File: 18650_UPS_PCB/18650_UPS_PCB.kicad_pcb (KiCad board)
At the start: 4 copper layers, 90 x 22 mm, 54 parts, among them J1 USB_B_Micro, J2 Conn_02x04_Odd_Even, J3 USB_A, SW1 SW_SPDT, SW2 ALPSALPINE_SKRHADE011, SW3 SW_SPDT, SW4 SW_SPDT, SW5 SW_SPDT, U1 STLINK-V3MINI, U10 LR9102G-xx, U2 R5478, U3 STC4054, U4 FS8205A, U5 ME2188Cxx, U6 XC9236Axx, U7 INA219AxD, U8 SSD1306_128_32, U9 STM32F030F4Px

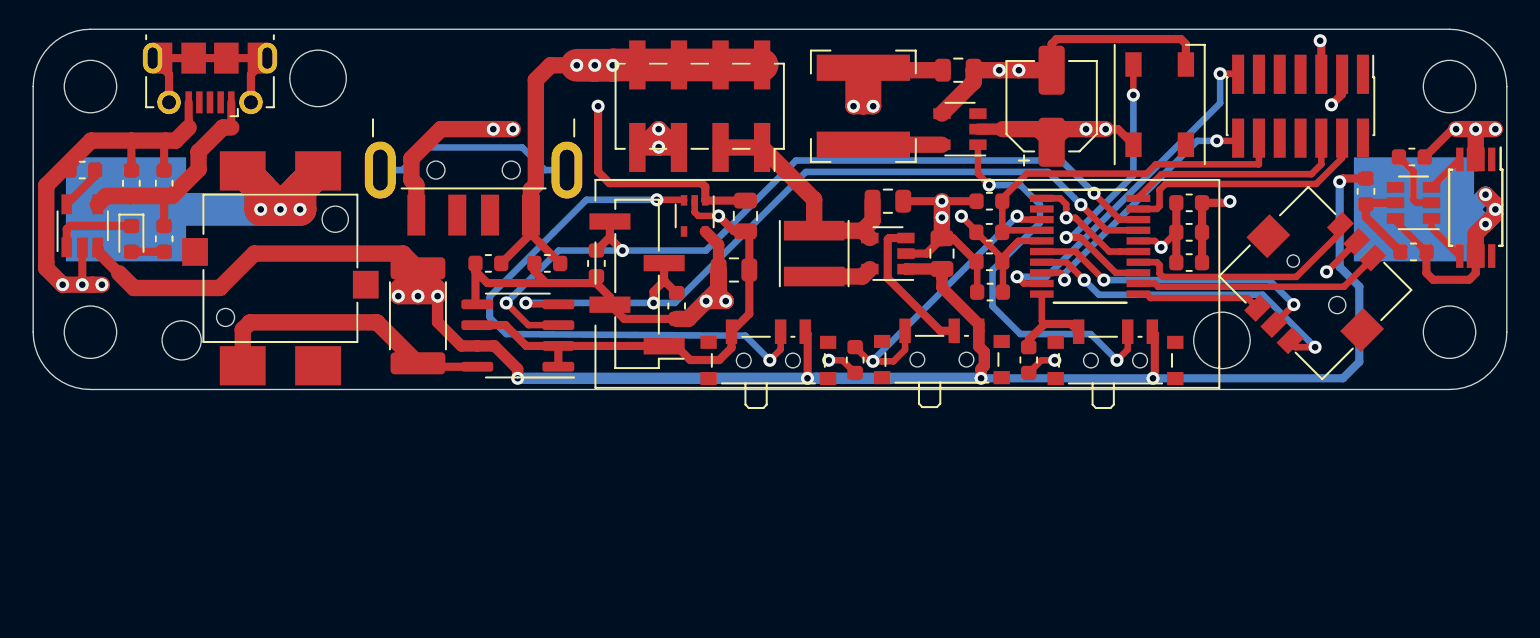
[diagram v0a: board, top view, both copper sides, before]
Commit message: base for v2 with new bms and sense ic
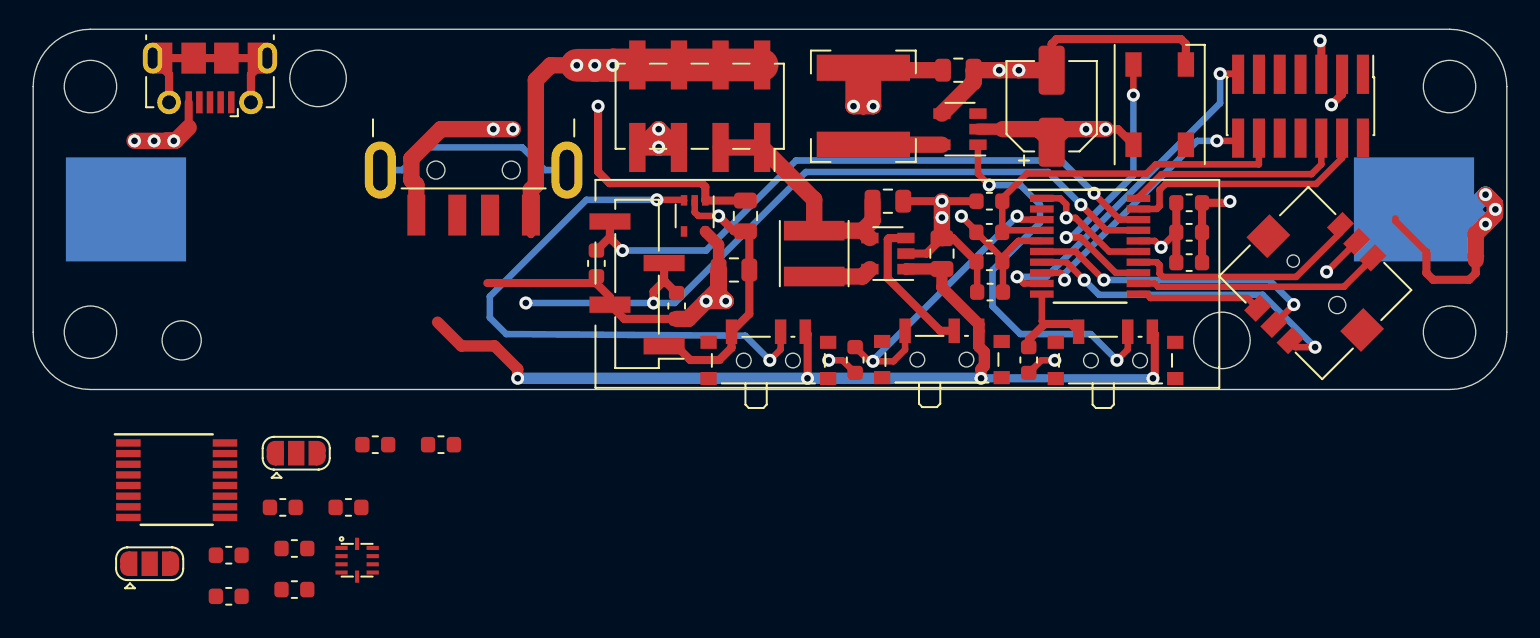
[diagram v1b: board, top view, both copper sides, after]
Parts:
- removed C12: 10 uF, Capacitor_SMD:C_0603_1608Metric
- removed C13: 100 nF, Capacitor_SMD:C_0603_1608Metric
- removed C2: 10 nF, Capacitor_SMD:C_0603_1608Metric
- removed C3: 1 uF, Capacitor_SMD:C_0603_1608Metric
- removed D1: LED_CHRG, LED_SMD:LED_0603_1608Metric
- removed R2: 0.1 Ohm, Resistor_SMD:R_2512_6332Metric
- removed R3, R4: 1 kOhm, Resistor_SMD:R_0603_1608Metric
- removed R5: 1.25 kOhm, Resistor_SMD:R_0603_1608Metric
- removed SW1: SW_SPDT, CUSTOM_FOOTPRINTS:ALPS_SPEF210101
- removed U3: STC4054, Package_TO_SOT_SMD:TSOT-23-5
- removed U4: FS8205A, Package_SO:TSSOP-8_4.4x3mm_P0.65mm
- removed U7: INA219AxD, Package_SO:SOIC-8_3.9x4.9mm_P1.27mm
- added C10: 1 uF, Capacitor_SMD:C_0603_1608Metric, F.Cu at (136.1, 103.4)
- added C11: 100 nF, Capacitor_SMD:C_0603_1608Metric, F.Cu at (141.7, 99.6)
- added C20: 10 uF, Capacitor_SMD:C_0603_1608Metric, F.Cu at (132.8, 108.8)
- added C21: 2.2 uF, Capacitor_SMD:C_0603_1608Metric, F.Cu at (136.8, 105.9)
- added JP1: SolderJumper_3_Open, Jumper:SolderJumper-3_P1.3mm_Open_RoundedPad1.0x1.5mm, F.Cu at (127.9, 106.8)
- added JP2: SolderJumper_3_Open, Jumper:SolderJumper-3_P1.3mm_Open_RoundedPad1.0x1.5mm, F.Cu at (136.9, 100.1)
- added R8: 10 kOhm, Resistor_SMD:R_0603_1608Metric, F.Cu at (145.7, 99.6)
- added R9: 10 kOhm, Resistor_SMD:R_0603_1608Metric, F.Cu at (136.8, 108.4)
- added U11: MP2667, CUSTOM_FOOTPRINTS:QFN-10-MP2667, F.Cu at (140.6, 106.6)
- R1: value 330 Ohm -> 10 kOhm
- U2: value R5478 -> INA260; footprint Package_TO_SOT_SMD:SOT-23-6 -> Package_SO:TSSOP-16_4.4x5mm_P0.65mm
- moved U2 77.4 mm to (129.6, 101.7), turned to 0 degrees
- moved R1 65.1 mm to (140.1, 103.4), turned to 0 degrees
- moved C1 23.5 mm to (132.8, 106.3), turned to 0 degrees
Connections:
- BT1 pad 2: -BATT -> GND
- C1 pad 1: -BATT -> +3.3VA
- C1 pad 2: VCC -> GND
- C14 pad 1: GNDD -> GND
- C15 pad 1: GNDD -> GND
- C16 pad 1: GNDD -> GND
- C17 pad 1: GNDD -> GND
- C18 pad 2: GNDD -> GND
- C19 pad 2: GNDD -> GND
- C4 pad 1: Shunt- -> IN-
- C4 pad 2: GNDD -> GND
- C5 pad 1: Shunt- -> IN-
- C5 pad 2: GNDD -> GND
- C6 pad 1: Shunt- -> IN-
- C6 pad 2: GNDD -> GND
- C7 pad 2: GNDD -> GND
- C8 pad 2: GNDD -> GND
- C9 pad 2: GNDD -> GND
- D2 pad 2: Net-(D2-Pad2) -> (no net)
- D2 pad 3: GNDD -> GND
- J1 pad 1: VCC -> Net-(C10-Pad1)
- J1 pad 2: Net-(J1-Pad2) -> (no net)
- J1 pad 3: Net-(J1-Pad3) -> (no net)
- J1 pad 4: Net-(J1-Pad4) -> (no net)
- J1 pad 5: -BATT -> GND
- J2 pad 2: GNDD -> GND
- J2 pad 4: GNDD -> GND
- J2 pad 6: GNDD -> GND
- J2 pad 8: GNDD -> GND
- J3 pad 2: Net-(J3-Pad2) -> (no net)
- J3 pad 3: Net-(J3-Pad3) -> (no net)
- J3 pad 4: GNDD -> GND
- L1 pad 1: Shunt- -> IN-
- R1 pad 1: Net-(C2-Pad2) -> +3.3VA
- R1 pad 2: Shunt- -> PF0
- R6 pad 2: GNDD -> GND
- R7 pad 2: GNDD -> GND
- SW2 pad 5: GNDD -> GND
- SW3 pad 3: Shunt- -> IN-
- SW4 pad 3: Shunt- -> IN-
- SW5 pad 1: GNDD -> GND
- SW5 pad 3: Shunt- -> IN-
- U1 pad 1: Net-(U1-Pad1) -> (no net)
- U1 pad 10: Net-(U1-Pad10) -> (no net)
- U1 pad 11: Net-(U1-Pad11) -> (no net)
- U1 pad 2: Net-(U1-Pad2) -> (no net)
- U1 pad 5: GNDD -> GND
- U1 pad 7: Net-(U1-Pad7) -> (no net)
- U1 pad 8: Net-(U1-Pad8) -> (no net)
- U1 pad 9: Net-(U1-Pad9) -> (no net)
- U10 pad 1: Shunt- -> IN-
- U10 pad 2: GNDD -> GND
- U10 pad 4: Net-(U10-Pad4) -> (no net)
- U2 pad 1: Net-(U2-Pad1) -> IN+
- U2 pad 2: Net-(R4-Pad2) -> IN+
- U2 pad 3: Net-(U2-Pad3) -> IN+
- U2 pad 5: Net-(C2-Pad2) -> Net-(JP1-Pad2)
- U2 pad 6: -BATT -> GND
- U5 pad 3: Net-(U5-Pad3) -> (no net)
- U5 pad 4: GNDD -> GND
- U6 pad 1: Shunt- -> IN-
- U6 pad 2: GNDD -> GND
- U8 pad 1: GNDD -> GND
- U9 pad 1: GNDD -> GND
- U9 pad 15: GNDD -> GND
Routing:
- net Shunt-: track 190.8 -> 0.00 mm, vias 11 -> 0
- net -BATT: track 143.4 -> 0.00 mm, vias 6 -> 0
- net IN-: track 0.00 -> 132.6 mm, vias 0 -> 7
- net GND: track 0.00 -> 128.6 mm, vias 0 -> 20
- net GNDD: track 123.0 -> 0.00 mm, vias 17 -> 0
- net Net-(BT1-Pad1): track 25.2 -> 0.00 mm, vias 3 -> 0
- net Shunt+: track 17.8 -> 0.00 mm
- net VCC: track 14.1 -> 0.00 mm
- net I2C1_SDA: track 50.7 -> 38.6 mm, vias 3 -> 2
- net +3.3VA: track 97.5 -> 91.8 mm
- net Net-(C2-Pad2): track 5.62 -> 0.00 mm
- net Net-(D1-Pad1): track 5.14 -> 0.00 mm
- net Net-(R4-Pad2): track 4.17 -> 0.00 mm
- net Net-(U2-Pad1): track 3.01 -> 0.00 mm
- net Net-(R5-Pad1): track 2.81 -> 0.00 mm
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- added copper zone on In1.Cu, net GND
- removed copper zone on In1.Cu, net GNDD

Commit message: savepoint before messing up pcbnew
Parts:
- removed D2: WS2812B, LED_SMD:LED_WS2812B_PLCC4_5.0x5.0mm_P3.2mm
- removed L2: 1.5 uH, Inductor_SMD:L_Taiyo-Yuden_MD-4040
- removed R12, R13, R17, R6, R7: 10 kOhm, Resistor_SMD:R_0603_1608Metric
- removed SW2: ALPSALPINE_SKRHADE011, CUSTOM_FOOTPRINTS:SKRHADE011
- removed SW3, SW4, SW5: SW_SPDT, Button_Switch_SMD:SW_SPDT_PCM12
- removed U6: XC9236Axx, Package_TO_SOT_SMD:SOT-23-5
- removed U8: SSD1306_128_32, Connector_PinHeader_2.54mm:PinHeader_1x04_P2.54mm_Vertical_SMD_Pin1Left
- removed U9: STM32F030F4Px, Package_SO:TSSOP-20_4.4x6.5mm_P0.65mm
- added C12: 100 nF, Capacitor_SMD:C_0603_1608Metric, F.Cu at (207.2, 161.4)
- added C13: 2.2 uF, Capacitor_SMD:C_0603_1608Metric, F.Cu at (187.8, 162.7)
- added C2: 1 uF, Capacitor_SMD:C_0603_1608Metric, F.Cu at (227.2, 157.7)
- added C3: 1 uF, Capacitor_SMD:C_0603_1608Metric, F.Cu at (199.2, 158.9)
- added J4: Conn_01x02, Connector_PinSocket_2.54mm:PinSocket_1x02_P2.54mm_Vertical, F.Cu at (228.6, 151.6)
- added J5: Conn_01x02, Connector_PinSocket_2.54mm:PinSocket_1x02_P2.54mm_Vertical, F.Cu at (240.4, 137.8)
- added J6: Conn_01x02, Connector_PinSocket_2.54mm:PinSocket_1x02_P2.54mm_Vertical, F.Cu at (222.9, 157.5)
- added JP3: EA_ADR, Jumper:SolderJumper-3_P1.3mm_Open_RoundedPad1.0x1.5mm, F.Cu at (188.7, 159.4)
- added JP4: TPS_LBI, Jumper:SolderJumper-3_P1.3mm_Open_RoundedPad1.0x1.5mm, F.Cu at (194.3, 159.4)
- added R2: 10 kOhm, Resistor_SMD:R_0603_1608Metric, F.Cu at (232.0, 146.0)
- added S1: TM-2027, CUSTOM_FOOTPRINTS:TM-2027, F.Cu at (223.0, 143.6)
- added SW1: SW_DIP_x02, CUSTOM_FOOTPRINTS:TS6637TP-4P, F.Cu at (180.5, 160.7)
- added U3: EA_DOGS164N-A, CUSTOM_FOOTPRINTS:EA_DOGS164N-A, F.Cu at (183.9, 155.6)
- added U4: TPS61032, Package_SO:HTSSOP-16-1EP_4.4x5mm_P0.65mm_EP3.4x5mm, F.Cu at (234.0, 141.4)
- C15: value 200 nF -> 220 uF; footprint Capacitor_SMD:C_0603_1608Metric -> Capacitor_Tantalum_SMD:CP_EIA-7343-43_Kemet-X_Pad2.25x2.55mm_HandSolder
- C16: value 200 nF -> 100 nF
- C17: value 4.7 uF -> 100 nF
- C18: value 10 nF -> 1 uF
- C19: value 1 uF -> 100 nF
- C4: value 4.7 uF -> 10 uF; footprint Capacitor_SMD:C_0805_2012Metric -> Capacitor_SMD:C_0603_1608Metric
- C5: value 10 uF -> 0.1 uF; footprint Capacitor_SMD:C_0805_2012Metric -> Capacitor_SMD:C_0603_1608Metric
- C7: value 100 uF -> 4.7 uF; footprint Capacitor_SMD:CP_Elec_5x5.4 -> Capacitor_SMD:C_0603_1608Metric
- C9: value 10 uF -> 100 nF; footprint Capacitor_SMD:C_0805_2012Metric -> Capacitor_SMD:C_0603_1608Metric
- J2: value Conn_02x04_Odd_Even -> Conn_01x02; footprint Connector_PinSocket_2.54mm:PinSocket_2x04_P2.54mm_Vertical_SMD -> Connector_PinSocket_2.54mm:PinSocket_1x02_P2.54mm_Vertical
- JP1: value SolderJumper_3_Open -> INA_ADR_0
- JP2: value SolderJumper_3_Open -> INA_ADR_1
- L1: value 22 uH -> 6.8 uH; footprint Inductor_SMD:L_Bourns-SRN6028 -> Inductor_SMD:L_10.4x10.4_H4.8
- U5: value ME2188Cxx -> STM32L151RCTx; footprint Package_TO_SOT_SMD:SOT-23-5 -> Package_QFP:LQFP-64_10x10mm_P0.5mm
- moved J2 97.0 mm to (218.3, 157.5), turned to 0 degrees
- moved C5 87.5 mm to (207.2, 158.9)
- moved C7 84.1 mm to (199.2, 161.4), turned to 0 degrees
- moved C19 82.9 mm to (244.7, 139.2), turned to 0 degrees
- moved L1 82.5 mm to (236.7, 129.5), turned to 0 degrees
- moved C9 82.4 mm to (203.2, 161.4)
- moved C18 80.2 mm to (244.7, 136.7), turned to 0 degrees
- moved C17 79.1 mm to (211.2, 161.4), turned to 0 degrees
- moved C14 79.1 mm to (191.9, 162.7)
- moved C4 75.9 mm to (203.2, 158.9), turned to 0 degrees
- moved C16 75.0 mm to (211.2, 158.9), turned to 0 degrees
- moved C15 70.4 mm to (221.1, 152.2), turned to 0 degrees
- moved U5 68.2 mm to (223.2, 130.8), turned to 0 degrees
- moved C20 34.9 mm to (148.3, 140.1)
- moved R9 34.9 mm to (152.3, 139.7)
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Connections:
- C1 pad 1: +3.3VA -> +3V3
- C14 pad 1: GND -> +3V3
- C14 pad 2: NRST -> GND
- C15 pad 1: GND -> +5V
- C15 pad 2: +3.3VA -> GND
- C16 pad 1: GND -> +3V3
- C16 pad 2: +3.3VA -> GND
- C17 pad 1: GND -> +3V3
- C17 pad 2: +3.3VA -> GND
- C18 pad 1: +3.3VA -> +3V3
- C19 pad 1: +3.3VA -> IN-
- C5 pad 1: IN- -> NRST
- C7 pad 1: +5V -> +3V3
- C8 pad 1: +3.3VA -> +3V3
- JP1 pad 3: +3.3VA -> +3V3
- JP2 pad 1: +3.3VA -> +3V3
- R1 pad 1: +3.3VA -> +3V3
- R1 pad 2: PF0 -> INA-ALERT
- U1 pad 3: +3.3VA -> +3V3
- U10 pad 3: LDOCE -> IN-
- U10 pad 5: +3.3VA -> +3V3
- U11 pad 3: (no net) -> MP-INT
- U2 pad 10: +3.3VA -> +3V3
- U2 pad 7: PF0 -> INA-ALERT
- U5 pad 1: BoostCE -> (no net)
- U5 pad 2: +5V -> (no net)
- U5 pad 4: GND -> (no net)
- U5 pad 5: Net-(L1-Pad2) -> (no net)
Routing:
- net +3V3: track 14.6 -> 106.4 mm, vias 0 -> 5
- net +3.3VA: track 91.8 -> 0.00 mm, vias 5 -> 0
- net LDOCE: track 35.8 -> 0.00 mm, vias 2 -> 0
- net IN-: track 132.6 -> 168.3 mm, vias 7 -> 9

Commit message: all parts on pcb
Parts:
- removed J3: USB_A, Connector_USB:USB_A_CNCTech_1001-011-01101_Horizontal
- JP3, JP4: moved to B.Cu
- U3: value EA_DOGS164N-A -> EA_DOGS104N-A; footprint CUSTOM_FOOTPRINTS:EA_DOGS164N-A -> CUSTOM_FOOTPRINTS:EA_DOGS104N-A
- moved C2 110.6 mm to (150.0, 78.4), turned to 180 degrees
- moved C18 103.3 mm to (148.3, 99.5), turned to 270 degrees
- moved JP3 102.2 mm to (129.7, 76.0), turned to 180 degrees
- moved R2 100.6 mm to (142.8, 99.5), turned to 90 degrees
- moved C16 99.7 mm to (136.5, 92.8), turned to 180 degrees
- moved J2 97.0 mm to (165.8, 75.9), turned to 90 degrees
- moved C14 96.8 mm to (142.3, 79.5), turned to 90 degrees
- moved J6 92.8 mm to (178.5, 75.9), turned to 90 degrees
- moved J5 92.1 mm to (172.2, 75.9), turned to 90 degrees
- moved C3 91.7 mm to (155.2, 78.4), turned to 180 degrees
- moved C12 91.4 mm to (156.4, 85.3)
- moved U5 87.7 mm to (146.0, 89.1), turned to 90 degrees
- moved J4 87.4 mm to (184.9, 75.9), turned to 90 degrees
- moved C17 86.6 mm to (150.6, 99.5), turned to 270 degrees
- moved C5 85.8 mm to (145.2, 99.5), turned to 270 degrees
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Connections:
- C10 pad 1: Net-(C10-Pad1) -> VBUS
- J1 pad 1: Net-(C10-Pad1) -> VBUS
- R8 pad 1: (no net) -> VBUS
- U11 pad 1: Net-(C10-Pad1) -> VBUS
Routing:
- net IN-: track 168.3 -> 0.00 mm, vias 9 -> 0
- net GND: track 128.6 -> 0.00 mm, vias 20 -> 0
- net +3V3: track 106.4 -> 0.00 mm, vias 5 -> 0
- net +5V: track 68.2 -> 0.00 mm, vias 6 -> 0
- net I2C1_SCL: track 46.1 -> 0.00 mm, vias 3 -> 0
- net I2C1_SDA: track 38.6 -> 0.00 mm, vias 2 -> 0
- net BoostCE: track 24.7 -> 0.00 mm, vias 2 -> 0
- net NRST: track 22.7 -> 0.00 mm
- net USART1_RX: track 21.4 -> 0.00 mm, vias 2 -> 0
- net PA1: track 20.6 -> 0.00 mm, vias 2 -> 0
- net PF1: track 19.0 -> 0.00 mm, vias 2 -> 0
- net PA0: track 18.5 -> 0.00 mm, vias 2 -> 0
- net PA7: track 17.7 -> 0.00 mm, vias 2 -> 0
- net USART1_TX: track 16.1 -> 0.00 mm, vias 2 -> 0
- net SWDIO: track 15.5 -> 0.00 mm
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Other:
- board size 90 x 22 mm -> 90 x 27.5 mm

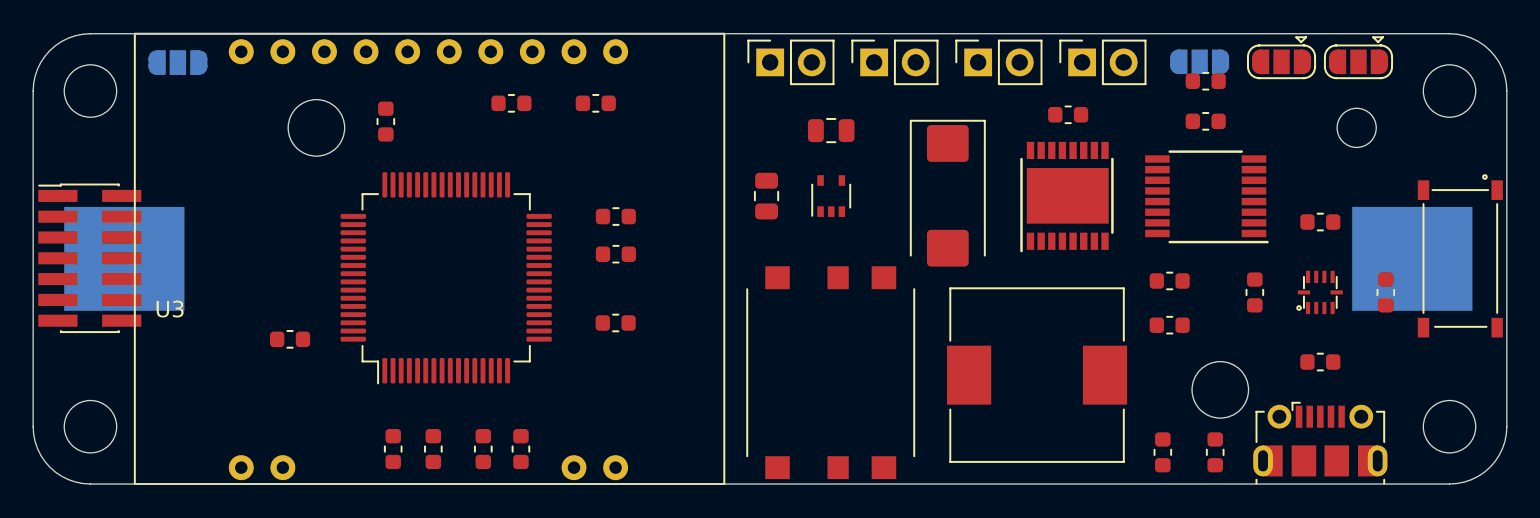
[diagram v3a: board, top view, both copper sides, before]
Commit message: placed all components
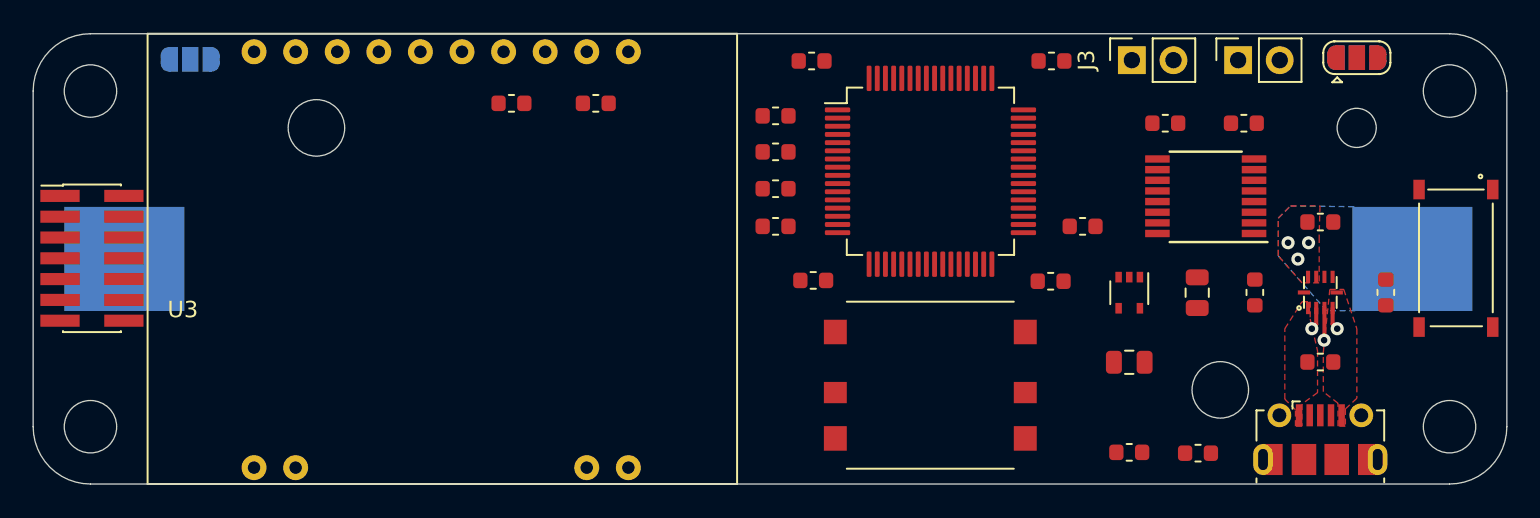
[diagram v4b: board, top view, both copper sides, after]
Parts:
- removed C13: 2.2 uF, Capacitor_SMD:C_0603_1608Metric
- removed C15: 220 uF, Capacitor_Tantalum_SMD:CP_EIA-7343-43_Kemet-X_Pad2.25x2.55mm_HandSolder
- removed C19: 100 nF, Capacitor_SMD:C_0603_1608Metric
- removed C4: 10 uF, Capacitor_SMD:C_0603_1608Metric
- removed J4, J5, J6: Conn_01x02, Connector_PinSocket_2.54mm:PinSocket_1x02_P2.54mm_Vertical
- removed JP4: TPS_LBI, Jumper:SolderJumper-3_P1.3mm_Open_RoundedPad1.0x1.5mm
- removed L1: 6.8 uH, Inductor_SMD:L_10.4x10.4_H4.8
- removed U4: TPS61032, Package_SO:HTSSOP-16-1EP_4.4x5mm_P0.65mm_EP3.4x5mm
- added J3: Conn_01x02, Connector_PinSocket_2.54mm:PinSocket_1x02_P2.54mm_Vertical, F.Cu at (187.9, 75.8)
- JP2: moved to B.Cu
- moved C14 40.8 mm to (183.0, 75.8), turned to 0 degrees
- moved C16 36.1 mm to (168.3, 75.8)
- moved R2 31.0 mm to (166.2, 79.2), turned to 0 degrees
- moved U5 30.3 mm to (175.6, 82.6), turned to 0 degrees
- moved J2 28.6 mm to (194.4, 75.8)
- moved C7 28.6 mm to (184.9, 86.0)
- moved C5 27.7 mm to (166.2, 81.4), turned to 180 degrees
- moved C6 27.0 mm to (191.9, 90.0), turned to 270 degrees
- moved C12 26.8 mm to (182.9, 89.3)
- moved C18 23.9 mm to (166.2, 83.7), turned to 180 degrees
- moved C8 23.1 mm to (187.8, 94.2), turned to 180 degrees
- moved C17 20.7 mm to (166.2, 86.0), turned to 180 degrees
- moved U10 19.1 mm to (187.8, 90.0), turned to 270 degrees
- moved C9 12.3 mm to (168.4, 89.2), turned to 180 degrees
- moved S1 6.13 mm to (175.6, 95.7), turned to 0 degrees
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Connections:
- U5 pad 20: TPS-SYNC -> (no net)
- U5 pad 21: TPS-EN -> (no net)
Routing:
- net MP-INT: track 0.00 -> 1.97 mm, vias 0 -> 1
- net Net-(C11-Pad1): track 0.00 -> 1.38 mm, vias 0 -> 1
- net Net-(R8-Pad2): track 0.00 -> 1.38 mm, vias 0 -> 1
- net Net-(BT1-Pad1): vias 0 -> 3
- added copper zone on F.Cu, net GND
- added copper zone on B.Cu, net Net-(BT1-Pad1)
- added copper zone on F.Cu, net Net-(BT1-Pad1)
- added copper zone on F.Cu, net VBUS
